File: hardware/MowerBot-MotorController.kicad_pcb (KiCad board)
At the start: 2 copper layers, 80 x 60 mm, 19 parts, among them J1 BTS7960_Left, J2 BTS7960_Right, J3 Encoder_Left, J4 Encoder_Right, J6 I2C_Expansion, J7 12V_Input, U1A ESP32_Left, U1B ESP32_Right, U2 LM2596_Module

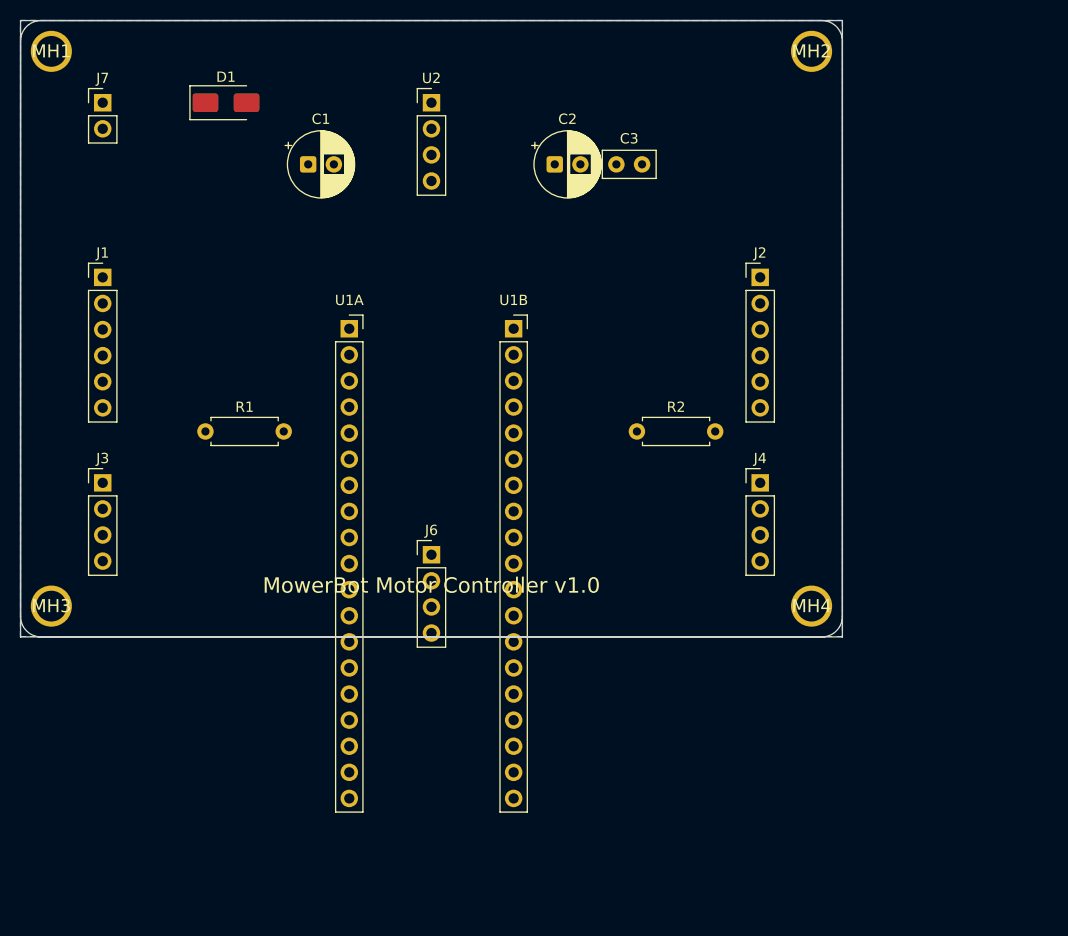
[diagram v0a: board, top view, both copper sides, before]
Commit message: fix: enlarge PCB to 100x80mm, reposition all components
The previous 80x60mm board was too small - ESP32 DevKit V1 pin headers
(48mm long) extended beyond the board edge. Also corrected ESP32 from
2x15-pin to 2x19-pin headers (38-pin DevKit).

Changes:
- Board size: 80x60mm -> 100x80mm
- Board outline: rounded rectangle with 2mm corner radius
- ESP32 headers: 2x Conn_01x19 (was 2x Conn_01x15)
- Mounting holes repositioned to new corners (4mm from edges)
- All components repositioned with proper spacing:
  - Power supply section (J7, D1, U2, C1, C2, C3) along top edge
  - ESP32 (U1A, U1B) centered
  - BTS7960 connectors (J1, J2) on left/right edges
  - Encoder connectors (J3, J4) below BTS7960
  - Pull-down resistors (R1, R2) between connectors and ESP32
  - I2C expansion (J6) at bottom center
  - Board text at bottom

Traces still need routing (manual or Freerouting).
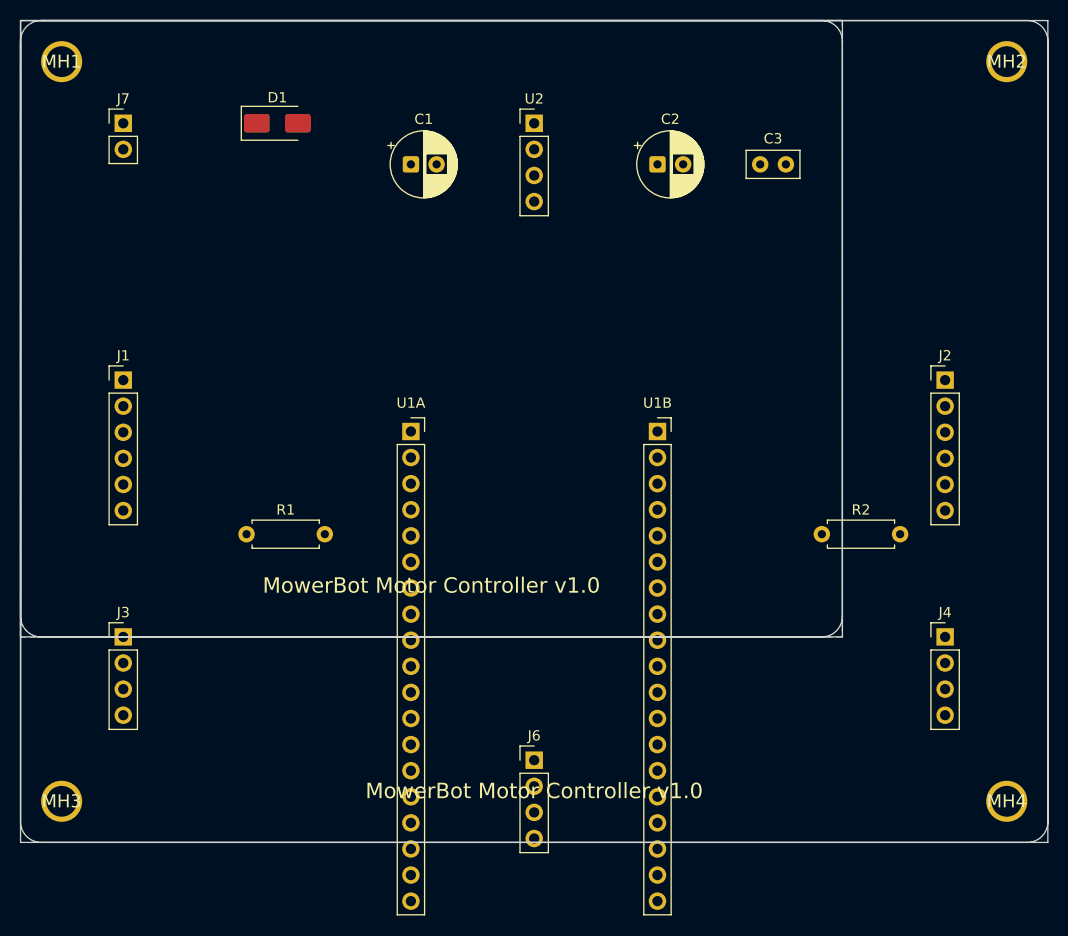
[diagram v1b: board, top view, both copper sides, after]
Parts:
- moved MH4 26.9 mm to (96.0, 76.0)
- moved J4 23.4 mm to (90.0, 60.0)
- moved J6 22.4 mm to (50.0, 72.0)
- moved J2 20.6 mm to (90.0, 35.0)
- moved R2 20.6 mm to (78.0, 50.0)
- moved MH2 19.0 mm to (96.0, 4.00)
- moved MH3 19.0 mm to (4.00, 76.0)
- moved U1B 17.2 mm to (62.0, 40.0)
- moved J3 15.1 mm to (10.0, 60.0)
- moved C3 14.0 mm to (72.0, 14.0)
- moved U1A 11.7 mm to (38.0, 40.0)
- moved R1 10.8 mm to (22.0, 50.0)
- moved J1 10.2 mm to (10.0, 35.0)
- moved U2 10.2 mm to (50.0, 10.0)
- moved C1 10.0 mm to (38.0, 14.0)
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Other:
- board size 80 x 60 mm -> 100 x 80 mm
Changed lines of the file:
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@@
 	(footprint "Connector_PinHeader_2.54mm:PinHeader_1x02_P2.54mm_Vertical"
 		(layer "F.Cu")
-		(at 8 8)
+		(at 10 10)
 		(descr "Through hole straight pin header, 1x02, 2.54mm pitch, single row")
 		(tags "Through hole pin header THT 1x02 2.54mm single row")
@@
 	(footprint ""
 		(layer "F.Cu")
-		(at 77 57)
+		(at 96 76)
 		(property "Reference" "MH4"
 			(at 0 0 0)
@@
 	(footprint "Connector_PinSocket_2.54mm:PinSocket_1x19_P2.54mm_Vertical"
 		(layer "F.Cu")
-		(at 48 30)
+		(at 62 40)
 		(descr "Through hole straight socket strip, 1x19, 2.54mm pitch, single row (from Kicad 4.0.7), script generated")
 		(tags "Through hole socket strip THT 1x19 2.54mm single row")
@@
 	(footprint "Connector_PinSocket_2.54mm:PinSocket_1x19_P2.54mm_Vertical"
 		(layer "F.Cu")
-		(at 32 30)
+		(at 38 40)
 		(descr "Through hole straight socket strip, 1x19, 2.54mm pitch, single row (from Kicad 4.0.7), script generated")
 		(tags "Through hole socket strip THT 1x19 2.54mm single row")
@@
 	(footprint "Resistor_THT:R_Axial_DIN0207_L6.3mm_D2.5mm_P7.62mm_Horizontal"
 		(layer "F.Cu")
-		(at 60 40)
+		(at 78 50)
 		(descr "Resistor, Axial_DIN0207 series, Axial, Horizontal, pin pitch=7.62mm, 0.25W = 1/4W, length*diameter=6.3*2.5mm^2, http://cdn-reichelt.de/documents/datenblatt/B400/1_4W%23YAG.pdf")
 		(tags "Resistor Axial_DIN0207 series Axial Horizontal pin pitch 7.62mm 0.25W = 1/4W length 6.3mm diameter 2.5mm")
@@
 	(footprint "Connector_PinHeader_2.54mm:PinHeader_1x04_P2.54mm_Vertical"
 		(layer "F.Cu")
-		(at 8 45)
+		(at 10 60)
 		(descr "Through hole straight pin header, 1x04, 2.54mm pitch, single row")
 		(tags "Through hole pin header THT 1x04 2.54mm single row")
@@
 	(footprint "Connector_PinHeader_2.54mm:PinHeader_1x04_P2.54mm_Vertical"
 		(layer "F.Cu")
-		(at 40 52)
+		(at 50 72)
 		(descr "Through hole straight pin header, 1x04, 2.54mm pitch, single row")
 		(tags "Through hole pin header THT 1x04 2.54mm single row")
@@
 	(footprint "Connector_PinHeader_2.54mm:PinHeader_1x06_P2.54mm_Vertical"
 		(layer "F.Cu")
-		(at 8 25)
+		(at 10 35)
 		(descr "Through hole straight pin header, 1x06, 2.54mm pitch, single row")
 		(tags "Through hole pin header THT 1x06 2.54mm single row")
@@
 	(footprint "Connector_PinHeader_2.54mm:PinHeader_1x04_P2.54mm_Vertical"
 		(layer "F.Cu")
-		(at 72 45)
+		(at 90 60)
 		(descr "Through hole straight pin header, 1x04, 2.54mm pitch, single row")
 		(tags "Through hole pin header THT 1x04 2.54mm single row")
@@
 	(footprint "Capacitor_THT:CP_Radial_D6.3mm_P2.50mm"
 		(layer "F.Cu")
-		(at 28 14)
+		(at 38 14)
 		(descr "CP, Radial series, Radial, pin pitch=2.50mm, diameter=6.3mm, height=7mm, Electrolytic Capacitor")
 		(tags "CP Radial series Radial pin pitch 2.50mm diameter 6.3mm height 7mm Electrolytic Capacitor")
@@
 	(footprint "Resistor_THT:R_Axial_DIN0207_L6.3mm_D2.5mm_P7.62mm_Horizontal"
 		(layer "F.Cu")
-		(at 18 40)
+		(at 22 50)
 		(descr "Resistor, Axial_DIN0207 series, Axial, Horizontal, pin pitch=7.62mm, 0.25W = 1/4W, length*diameter=6.3*2.5mm^2, http://cdn-reichelt.de/documents/datenblatt/B400/1_4W%23YAG.pdf")
 		(tags "Resistor Axial_DIN0207 series Axial Horizontal pin pitch 7.62mm 0.25W = 1/4W length 6.3mm diameter 2.5mm")
@@
 	(footprint "Capacitor_THT:CP_Radial_D6.3mm_P2.50mm"
 		(layer "F.Cu")
-		(at 52 14)
+		(at 62 14)
 		(descr "CP, Radial series, Radial, pin pitch=2.50mm, diameter=6.3mm, height=7mm, Electrolytic Capacitor")
 		(tags "CP Radial series Radial pin pitch 2.50mm diameter 6.3mm height 7mm Electrolytic Capacitor")
@@
 	(footprint ""
 		(layer "F.Cu")
-		(at 3 57)
+		(at 4 76)
 		(property "Reference" "MH3"
 			(at 0 0 0)
@@
 	(footprint "Capacitor_THT:C_Disc_D5.0mm_W2.5mm_P2.50mm"
 		(layer "F.Cu")
-		(at 58 14)
+		(at 72 14)
 		(descr "C, Disc series, Radial, pin pitch=2.50mm, diameter*width=5*2.5mm^2, Capacitor, http://cdn-reichelt.de/documents/datenblatt/B300/DS_KERKO_TC.pdf")
 		(tags "C Disc series Radial pin pitch 2.50mm diameter 5mm width 2.5mm Capacitor")
@@
 	(footprint ""
 		(layer "F.Cu")
-		(at 77 3)
+		(at 96 4)
 		(property "Reference" "MH2"
 			(at 0 0 0)
@@
 	(footprint "Diode_SMD:D_SMA"
 		(layer "F.Cu")
-		(at 20 8)
+		(at 25 10)
 		(descr "Diode SMA (DO-214AC)")
 		(tags "Diode SMA (DO-214AC)")
@@
 	(footprint ""
 		(layer "F.Cu")
-		(at 3 3)
+		(at 4 4)
 		(property "Reference" "MH1"
 			(at 0 0 0)
@@
 	(footprint "Connector_PinHeader_2.54mm:PinHeader_1x06_P2.54mm_Vertical"
 		(layer "F.Cu")
-		(at 72 25)
+		(at 90 35)
 		(descr "Through hole straight pin header, 1x06, 2.54mm pitch, single row")
 		(tags "Through hole pin header THT 1x06 2.54mm single row")
@@
 	(footprint "Connector_PinHeader_2.54mm:PinHeader_1x04_P2.54mm_Vertical"
 		(layer "F.Cu")
-		(at 40 8)
+		(at 50 10)
 		(descr "Through hole straight pin header, 1x04, 2.54mm pitch, single row")
 		(tags "Through hole pin header THT 1x04 2.54mm single row")
@@
 		(layer "Edge.Cuts")
 	)
+	(gr_line
+		(start 0 0)
+		(end 100 0)
+		(stroke
+			(width 0)
+			(type default)
+		)
+		(layer "Edge.Cuts")
+	)
 	(gr_arc
 		(start 0 2)
@@
 	)
 	(gr_line
+		(start 0 78)
+		(end 0 2)
+		(stroke
+			(width 0)
+			(type default)
+		)
+		(layer "Edge.Cuts")
+	)
+	(gr_line
+		(start 0 80)
+		(end 0 0)
+		(stroke
+			(width 0)
+			(type default)
+		)
+		(layer "Edge.Cuts")
+	)
+	(gr_line
 		(start 2 0)
 		(end 78 0)
@@
 		(layer "Edge.Cuts")
 	)
+	(gr_line
+		(start 2 0)
+		(end 98 0)
+		(stroke
+			(width 0)
+			(type default)
+		)
+		(layer "Edge.Cuts")
+	)
 	(gr_arc
 		(start 2 60)
@@
 	)
 	(gr_arc
+		(start 2 80)
+		(mid 0.585786 79.414214)
+		(end 0 78)
+		(stroke
+			(width 0)
+			(type default)
+		)
+		(layer "Edge.Cuts")
+	)
+	(gr_arc
 		(start 78 0)
 		(mid 79.414214 0.585786)
@@
 		(layer "Edge.Cuts")
 	)
+	(gr_arc
+		(start 98 0)
+		(mid 99.414214 0.585786)
+		(end 100 2)
+		(stroke
+			(width 0)
+			(type default)
+		)
+		(layer "Edge.Cuts")
+	)
+	(gr_line
+		(start 98 80)
+		(end 2 80)
+		(stroke
+			(width 0)
+			(type default)
+		)
+		(layer "Edge.Cuts")
+	)
+	(gr_line
+		(start 100 0)
+		(end 100 80)
+		(stroke
+			(width 0)
+			(type default)
+		)
+		(layer "Edge.Cuts")
+	)
+	(gr_line
+		(start 100 2)
+		(end 100 78)
+		(stroke
+			(width 0)
+			(type default)
+		)
+		(layer "Edge.Cuts")
+	)
+	(gr_arc
+		(start 100 78)
+		(mid 99.414214 79.414214)
+		(end 98 80)
+		(stroke
+			(width 0)
+			(type default)
+		)
+		(layer "Edge.Cuts")
+	)
+	(gr_line
+		(start 100 80)
+		(end 0 80)
+		(stroke
+			(width 0)
+			(type default)
+		)
+		(layer "Edge.Cuts")
+	)
 	(gr_text "MowerBot Motor Controller v1.0"
 		(at 40 55 0)
 		(layer "F.SilkS")
 		(effects
+			(font
+				(size 1.5 1.5)
+				(thickness 0.15)
+			)
+		)
+	)
+	(gr_text "MowerBot Motor Controller v1.0"
+		(at 50 75 0)
+		(layer "F.SilkS")
+		(effects

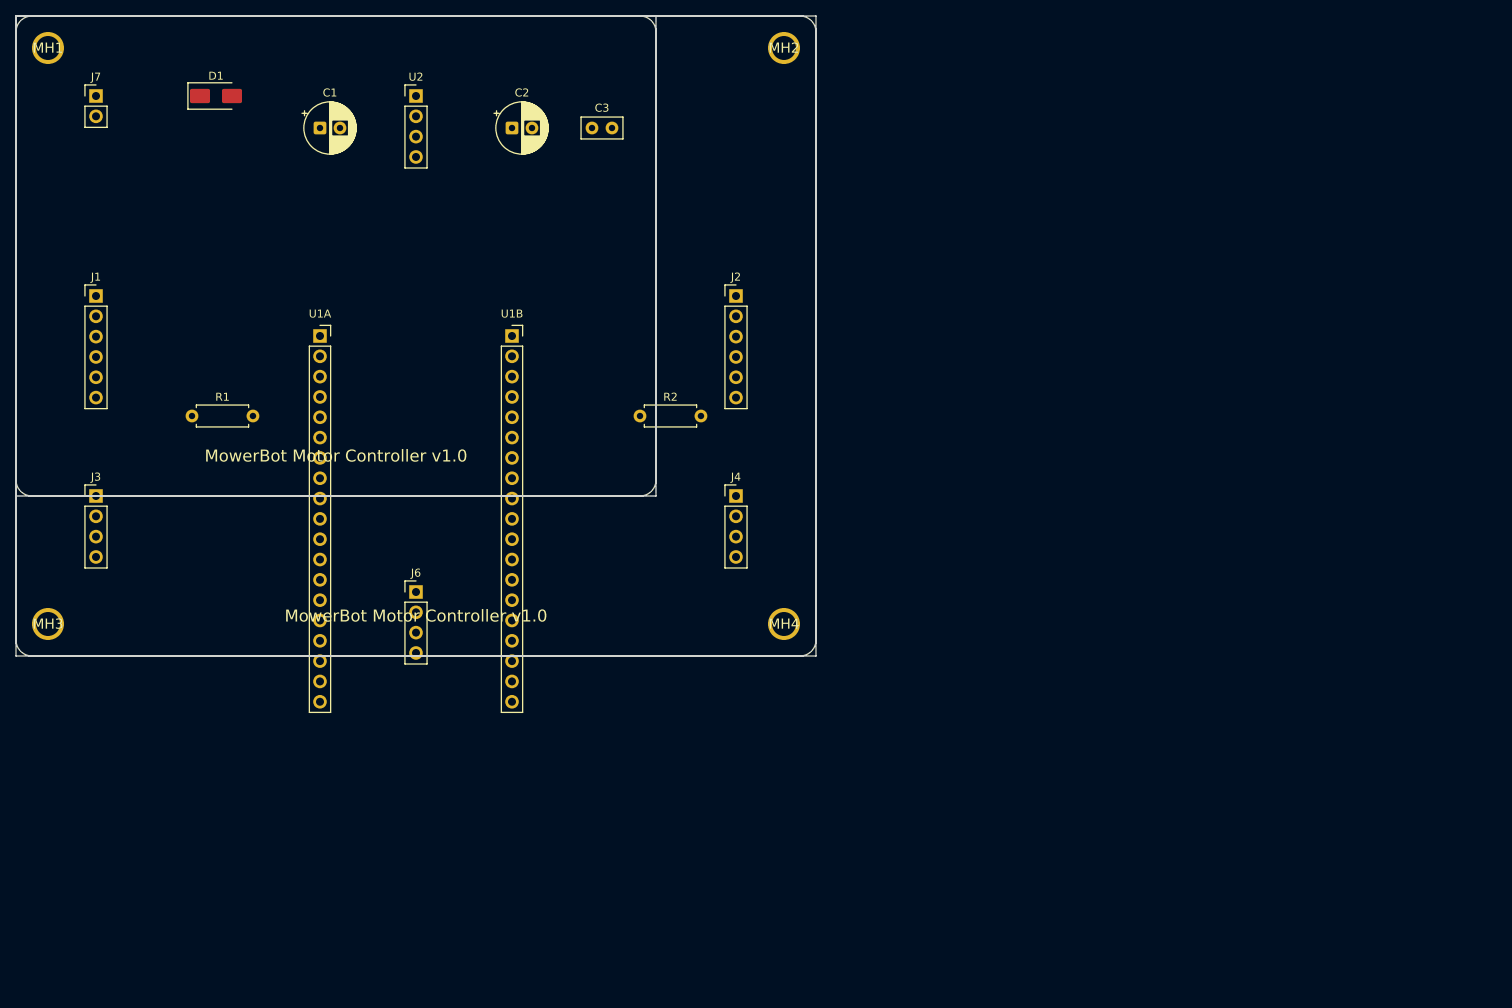
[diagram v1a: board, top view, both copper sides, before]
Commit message: feat: redesign PCB as Raspberry Pi HAT v2.0 (65x100mm)
Complete KiCad project redesign for Raspberry Pi HAT form factor.

Board specifications:
- Size: 65x100mm (Pi HAT width, extended length)
- 6x M2.5 mounting holes (4 Pi HAT standard + 2 chassis support)
- GND copper pour on B.Cu
- Stacking header for Pi GPIO pass-through

Components (15 total):
- J_PI: 2x20 Pin Socket (40-pin Stacking Header for Pi GPIO)
- U1A/U1B: 2x 1x15 Pin Socket (ESP32-C3-DevKitM-1)
- J_SIG_L/R: 1x6 Pin Header (BTS7960 signal connectors)
- J_PWR_L/R: 2-pin Screw Terminal (BTS7960 12V power, 5.08mm)
- J_ENC_L/R: 1x4 Pin Header (encoder connectors)
- J7: 2-pin Screw Terminal (12V input from XT60 cable)
- U2: 1x4 Pin Header (MINI560 5V/5A step-down module)
- C1: 100uF/25V electrolytic (12V buffer)
- C2: 100uF/16V electrolytic (5V buffer)
- C3: 100nF ceramic (ESP32 VIN decoupling)
- R1/R2: 10k resistors (pull-down for motor enable safety)

Net assignments:
- 12V, 5V, 3V3, GND power rails
- PI_TXD, PI_RXD (UART between Pi and ESP32-C3)
- MOT_L_RPWM, MOT_L_LPWM, MOT_L_EN (left motor)
- MOT_R_RPWM, MOT_R_LPWM, MOT_R_EN (right motor)
- ENC_L_A, ENC_L_B, ENC_R_A, ENC_R_B (encoders)

Note: Schematic net labels are placed but may need manual
refinement in KiCad. Traces need routing (Freerouting or manual).
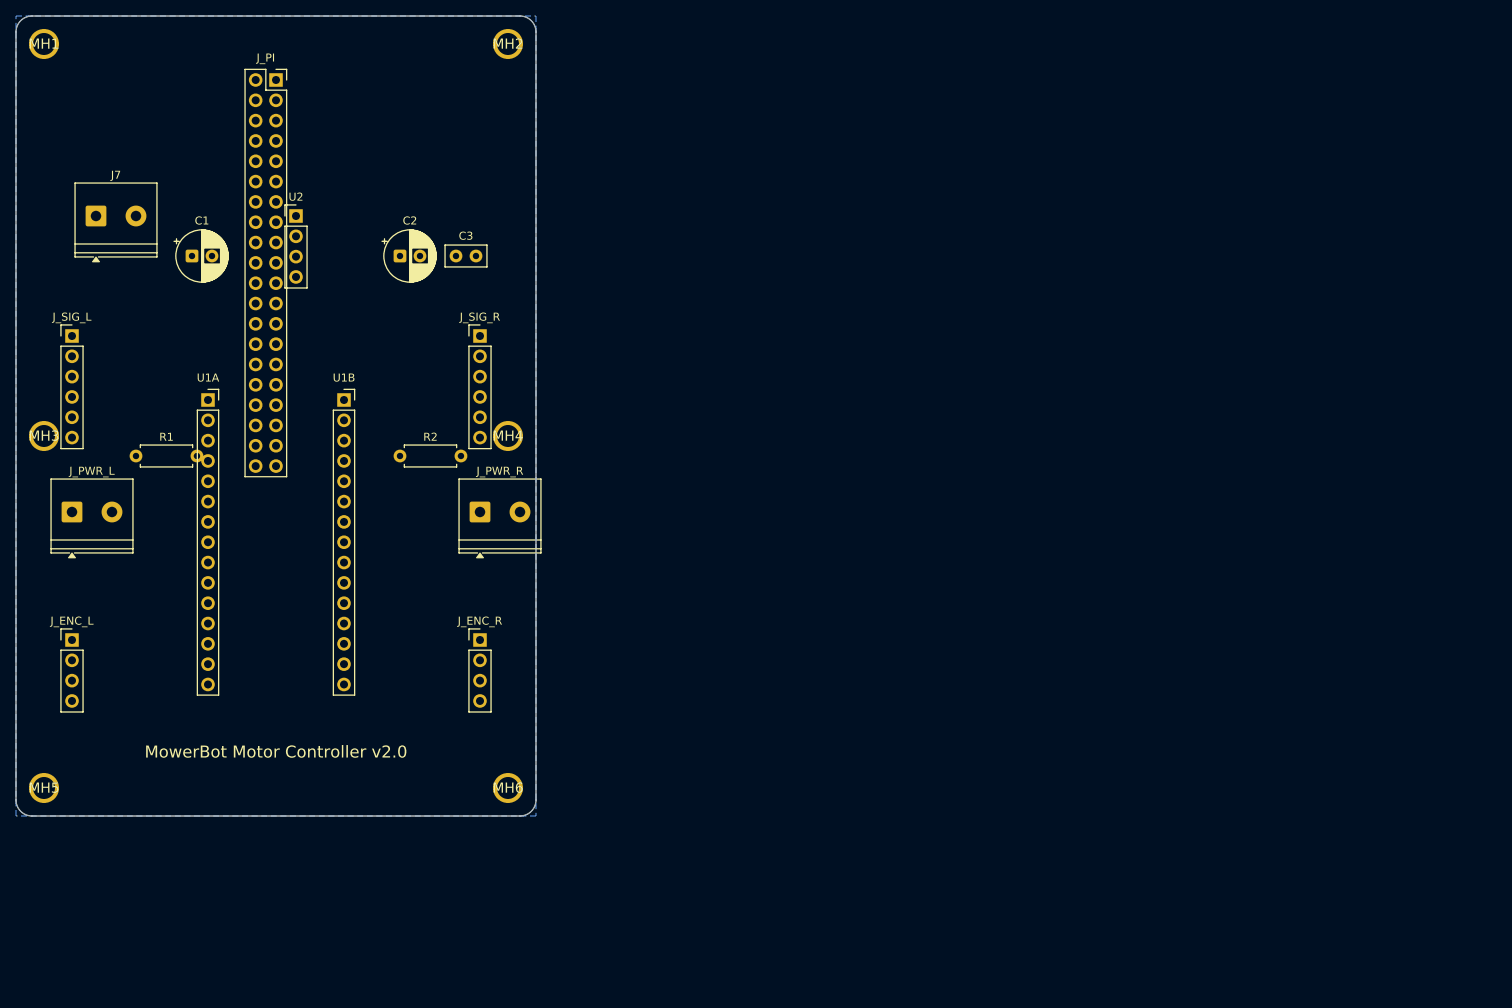
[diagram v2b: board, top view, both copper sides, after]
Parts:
- removed D1: SS34, Diode_SMD:D_SMA
- removed J1: BTS7960_Left, Connector_PinHeader_2.54mm:PinHeader_1x06_P2.54mm_Vertical
- removed J2: BTS7960_Right, Connector_PinHeader_2.54mm:PinHeader_1x06_P2.54mm_Vertical
- removed J3: Encoder_Left, Connector_PinHeader_2.54mm:PinHeader_1x04_P2.54mm_Vertical
- removed J4: Encoder_Right, Connector_PinHeader_2.54mm:PinHeader_1x04_P2.54mm_Vertical
- removed J6: I2C_Expansion, Connector_PinHeader_2.54mm:PinHeader_1x04_P2.54mm_Vertical
- removed the U1A at (38.0, 40.0)
- removed the U1B at (62.0, 40.0)
- added J_ENC_L: Encoder_Left, Connector_PinHeader_2.54mm:PinHeader_1x04_P2.54mm_Vertical, F.Cu at (7.00, 78.0)
- added J_ENC_R: Encoder_Right, Connector_PinHeader_2.54mm:PinHeader_1x04_P2.54mm_Vertical, F.Cu at (58.0, 78.0)
- added J_PI: RPi_GPIO_40Pin, Connector_PinSocket_2.54mm:PinSocket_2x20_P2.54mm_Vertical, F.Cu at (32.5, 8.00)
- added J_PWR_L: BTS7960_L_Power, TerminalBlock_Phoenix:TerminalBlock_Phoenix_PT-1,5-2-5.0-H_1x02_P5.00mm_Horizontal, F.Cu at (7.00, 62.0)
- added J_PWR_R: BTS7960_R_Power, TerminalBlock_Phoenix:TerminalBlock_Phoenix_PT-1,5-2-5.0-H_1x02_P5.00mm_Horizontal, F.Cu at (58.0, 62.0)
- added J_SIG_L: BTS7960_L_Signal, Connector_PinHeader_2.54mm:PinHeader_1x06_P2.54mm_Vertical, F.Cu at (7.00, 40.0)
- added J_SIG_R: BTS7960_R_Signal, Connector_PinHeader_2.54mm:PinHeader_1x06_P2.54mm_Vertical, F.Cu at (58.0, 40.0)
- added MH5: MountingHole_2.75mm, , F.Cu at (3.50, 96.5)
- added MH6: MountingHole_2.75mm, , F.Cu at (61.5, 96.5)
- added U1A: ESP32C3_J1, Connector_PinSocket_2.54mm:PinSocket_1x15_P2.54mm_Vertical, F.Cu at (24.0, 48.0)
- added U1B: ESP32C3_J3, Connector_PinSocket_2.54mm:PinSocket_1x15_P2.54mm_Vertical, F.Cu at (41.0, 48.0)
- J7: value 12V_Input -> 12V_XT60; footprint Connector_PinHeader_2.54mm:PinHeader_1x02_P2.54mm_Vertical -> TerminalBlock_Phoenix:TerminalBlock_Phoenix_PT-1,5-2-5.0-H_1x02_P5.00mm_Horizontal
- MH1, MH2, MH3, MH4: value MountingHole_3mm -> MountingHole_2.75mm
- U2: value LM2596_Module -> MINI560
- moved MH4 41.7 mm to (61.5, 52.5)
- moved MH2 34.5 mm to (61.5, 3.50)
- moved R2 30.4 mm to (48.0, 55.0)
- moved MH3 23.5 mm to (3.50, 52.5)
- moved C3 23.3 mm to (55.0, 30.0)
- moved C1 22.6 mm to (22.0, 30.0)
- moved C2 21.3 mm to (48.0, 30.0)
- moved U2 21.2 mm to (35.0, 25.0)
- moved J7 15.0 mm to (10.0, 25.0)
- moved R1 8.60 mm to (15.0, 55.0)
- moved MH1 0.71 mm to (3.50, 3.50)
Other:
- board size 100 x 80 mm -> 65 x 100 mm
- board text added: "MowerBot Motor Controller v2.0"
- board text removed: "MowerBot Motor Controller v1.0"
